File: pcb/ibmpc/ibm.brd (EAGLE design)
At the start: 104 x 74 mm, 43 parts, among them J2 ATX24RH

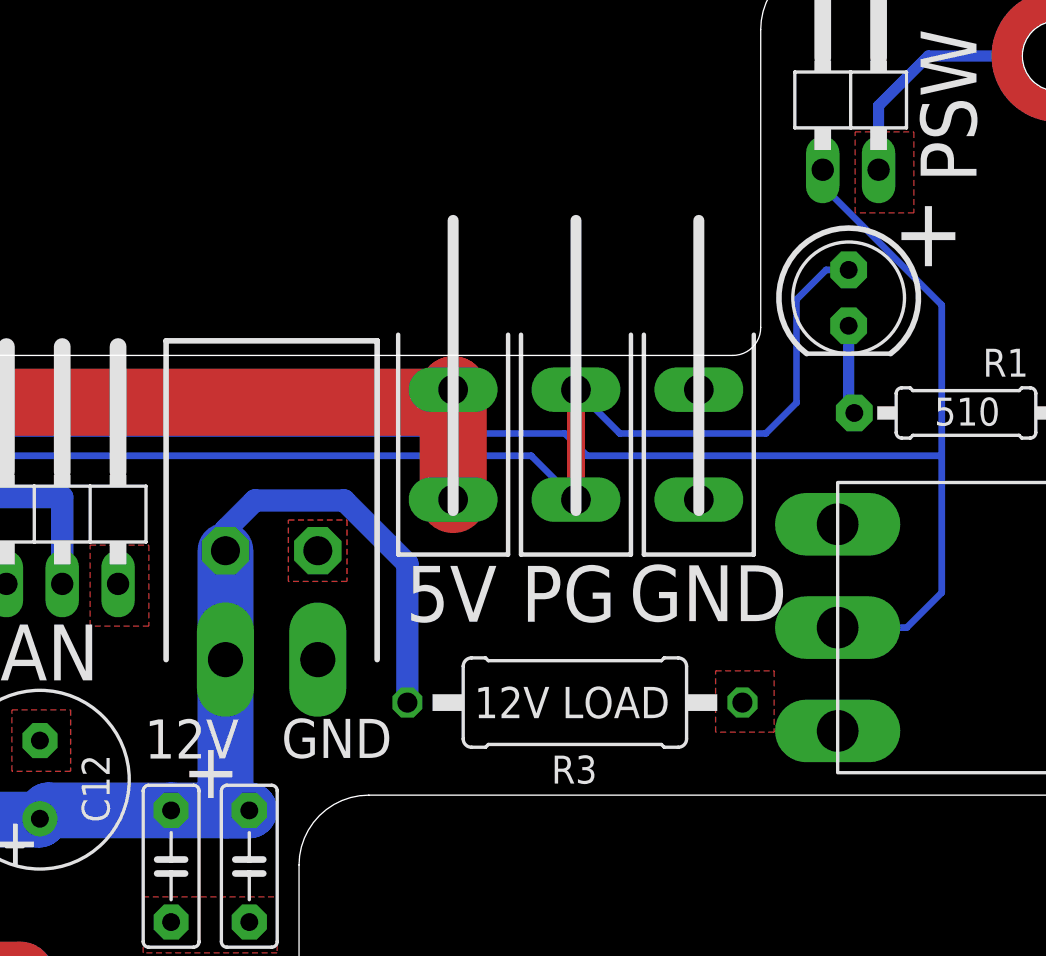
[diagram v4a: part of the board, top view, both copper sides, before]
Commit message: added 12V load resistor and blade
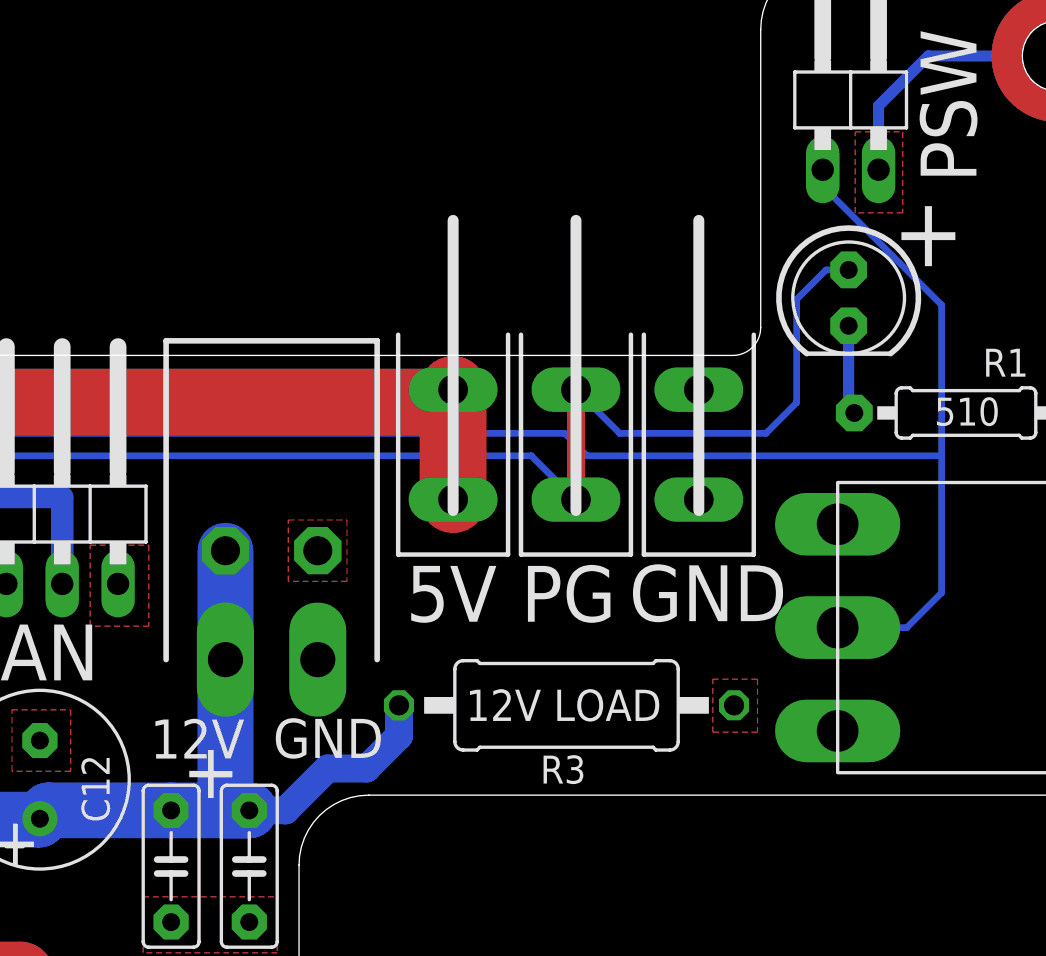
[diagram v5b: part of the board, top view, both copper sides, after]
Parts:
- moved R3 0.40 mm to (77.2, 40.1)
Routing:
- net +12V: track 121.4 -> 113.7 mm
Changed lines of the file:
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@@
 <text x="77.264" y="45.157" size="2.54" layer="25" align="center">PG</text>
 <text x="52.753" y="42.49" size="2.54" layer="25" align="center">FAN</text>
-<text x="60.119" y="38.553" size="1.778" layer="25" align="center">12V</text>
-<text x="66.717" y="38.58" size="1.778" layer="25" rot="R180" align="center">GND</text>
+<text x="60.373" y="38.553" size="1.778" layer="25" align="center">12V</text>
+<text x="66.336" y="38.58" size="1.778" layer="25" rot="R180" align="center">GND</text>
 <rectangle x1="69.469" y1="48.006" x2="74.549" y2="55.753" layer="41"/>
 <rectangle x1="75.184" y1="48.006" x2="80.264" y2="55.753" layer="41"/>
@@
 <text x="47.019" y="40.185" size="2.1844" layer="25" align="center">+</text>
 <text x="38.383" y="43.995" size="2.1844" layer="25" align="center">+</text>
-<text x="77.416" y="40.212" size="1.4224" layer="25" rot="R180" align="center">12V LOAD</text>
+<text x="77.035" y="40.085" size="1.4224" layer="25" rot="R180" align="center">12V LOAD</text>
 </plain>
 <attributes>
@@
 <attribute name="VALUE" x="59.944" y="34.798" size="1.27" layer="27" ratio="10" rot="R270"/>
 </element>
-<element name="R3" library="adafruit_changed" package="0411/15" value="" x="77.548" y="40.21" smashed="yes" rot="R180">
-<attribute name="NAME" x="78.564" y="37.797" size="1.27" layer="25" ratio="10" rot="R180"/>
-<attribute name="VALUE" x="81.1294" y="40.845" size="1.27" layer="27" ratio="10" rot="R180"/>
+<element name="R3" library="adafruit_changed" package="0411/15" value="" x="77.167" y="40.083" smashed="yes" rot="R180">
+<attribute name="NAME" x="78.056" y="37.797" size="1.27" layer="25" ratio="10" rot="R180"/>
+<attribute name="VALUE" x="80.7484" y="40.718" size="1.27" layer="27" ratio="10" rot="R180"/>
 </element>
 <element name="TP2" library="testpad" library_urn="urn:adsk.eagle:library:385" package="P1-13" package3d_urn="urn:adsk.eagle:package:27946/1" value="TPPAD1-13" x="61.654" y="47.117" smashed="yes">
@@
 <polygon width="0.1524" layer="1" thermals="no">
 <vertex x="90.297" y="66.167"/>
-<vertex x="92.964" y="66.167"/>
-<vertex x="92.964" y="62.484"/>
+<vertex x="92.456" y="66.167"/>
+<vertex x="92.456" y="62.484"/>
 <vertex x="90.297" y="62.484"/>
 </polygon>
@@
 </polygon>
 <polygon width="0.1524" layer="1" thermals="no">
-<vertex x="83.947" y="41.656"/>
-<vertex x="86.614" y="41.656"/>
-<vertex x="86.614" y="38.862"/>
-<vertex x="83.947" y="38.862"/>
+<vertex x="83.82" y="41.275"/>
+<vertex x="85.852" y="41.275"/>
+<vertex x="85.852" y="38.862"/>
+<vertex x="83.82" y="38.862"/>
 </polygon>
 </signal>
@@
 <contactref element="TP2" pad="TP"/>
 <wire x1="61.654" y1="42.164" x2="61.654" y2="47.117" width="2.54" layer="16"/>
-<wire x1="61.654" y1="47.117" x2="61.654" y2="48.065" width="1.016" layer="16"/>
-<wire x1="61.654" y1="48.065" x2="62.992" y2="49.403" width="1.016" layer="16"/>
-<wire x1="62.992" y1="49.403" x2="67.056" y2="49.403" width="1.016" layer="16"/>
-<wire x1="67.056" y1="49.403" x2="69.928" y2="46.531" width="1.016" layer="16"/>
-<wire x1="69.928" y1="46.531" x2="69.928" y2="40.21" width="1.016" layer="16"/>
+<wire x1="62.738" y1="35.306" x2="64.389" y2="35.306" width="1.27" layer="16"/>
+<wire x1="64.389" y1="35.306" x2="66.294" y2="37.211" width="1.27" layer="16"/>
+<wire x1="66.294" y1="37.211" x2="68.072" y2="37.211" width="1.27" layer="16"/>
+<wire x1="68.072" y1="37.211" x2="69.547" y2="38.686" width="1.27" layer="16"/>
+<wire x1="69.547" y1="38.686" x2="69.547" y2="40.083" width="1.27" layer="16"/>
 <wire x1="61.654" y1="42.037" x2="61.654" y2="42.164" width="0" layer="19" extent="16-16"/>
 </signal>

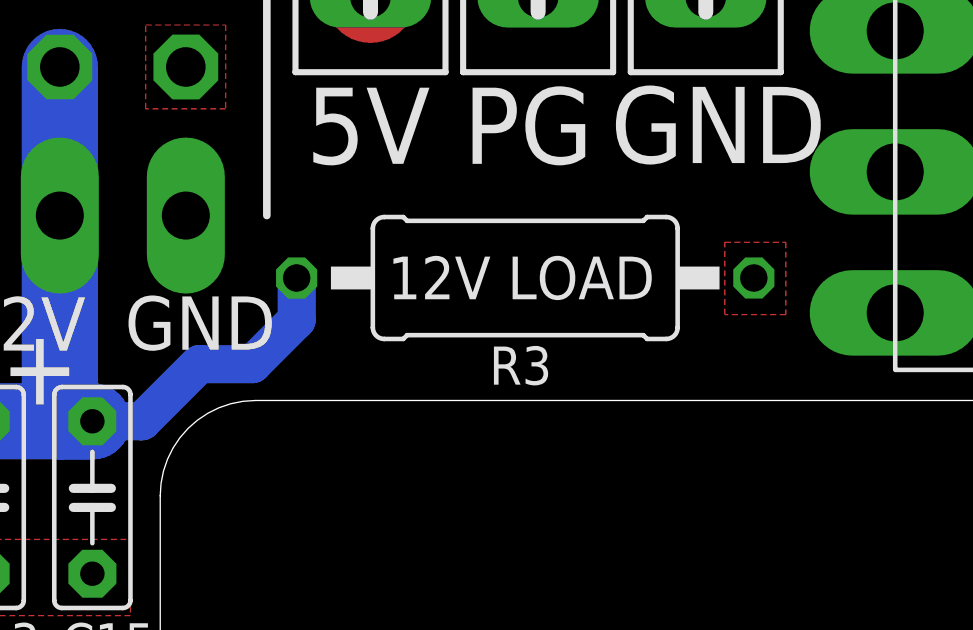
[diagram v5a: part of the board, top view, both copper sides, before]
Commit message: updated with more caps
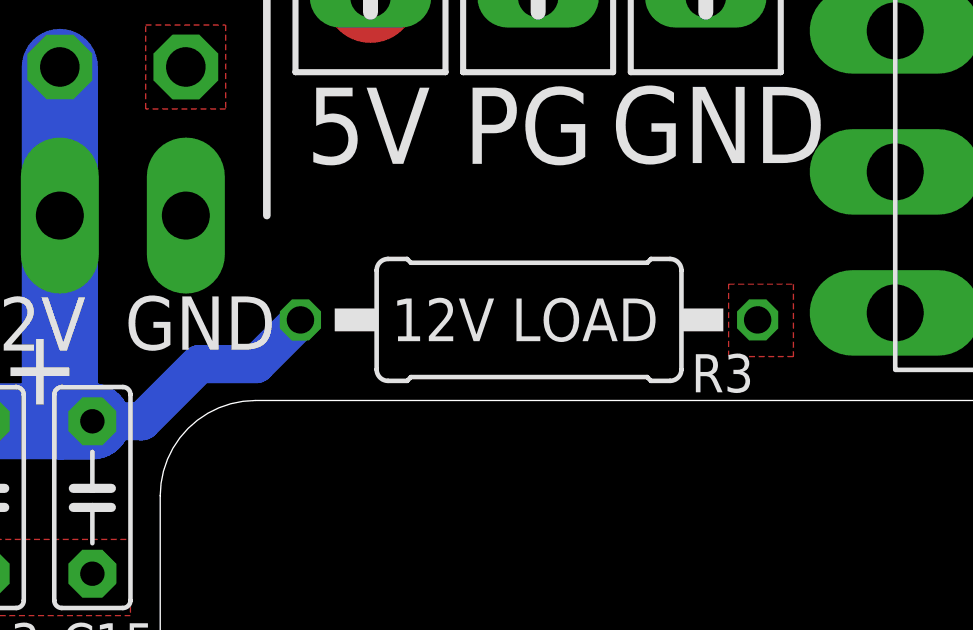
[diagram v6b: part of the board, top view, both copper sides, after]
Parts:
- moved R3 1.40 mm to (77.3, 38.7)
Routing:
- net +12V: track 113.7 -> 112.4 mm
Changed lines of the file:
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@@
 <text x="47.019" y="40.185" size="2.1844" layer="25" align="center">+</text>
 <text x="38.383" y="43.995" size="2.1844" layer="25" align="center">+</text>
-<text x="77.035" y="40.085" size="1.4224" layer="25" rot="R180" align="center">12V LOAD</text>
+<text x="77.162" y="38.688" size="1.4224" layer="25" rot="R180" align="center">12V LOAD</text>
 </plain>
 <attributes>
@@
 <attribute name="VALUE" x="59.944" y="34.798" size="1.27" layer="27" ratio="10" rot="R270"/>
 </element>
-<element name="R3" library="adafruit_changed" package="0411/15" value="" x="77.167" y="40.083" smashed="yes" rot="R180">
-<attribute name="NAME" x="78.056" y="37.797" size="1.27" layer="25" ratio="10" rot="R180"/>
-<attribute name="VALUE" x="80.7484" y="40.718" size="1.27" layer="27" ratio="10" rot="R180"/>
+<element name="R3" library="adafruit_changed" package="0411/15" value="" x="77.294" y="38.686" smashed="yes" rot="R180">
+<attribute name="NAME" x="84.787" y="37.543" size="1.27" layer="25" ratio="10" rot="R180"/>
+<attribute name="VALUE" x="80.8754" y="39.321" size="1.27" layer="27" ratio="10" rot="R180"/>
 </element>
 <element name="TP2" library="testpad" library_urn="urn:adsk.eagle:library:385" package="P1-13" package3d_urn="urn:adsk.eagle:package:27946/1" value="TPPAD1-13" x="61.654" y="47.117" smashed="yes">
@@
 </polygon>
 <polygon width="0.1524" layer="1" thermals="no">
-<vertex x="83.82" y="41.275"/>
-<vertex x="85.852" y="41.275"/>
-<vertex x="85.852" y="38.862"/>
-<vertex x="83.82" y="38.862"/>
+<vertex x="83.947" y="39.878"/>
+<vertex x="86.106" y="39.878"/>
+<vertex x="86.106" y="37.465"/>
+<vertex x="83.947" y="37.465"/>
 </polygon>
 </signal>
@@
 <wire x1="62.738" y1="35.306" x2="64.389" y2="35.306" width="1.27" layer="16"/>
 <wire x1="64.389" y1="35.306" x2="66.294" y2="37.211" width="1.27" layer="16"/>
-<wire x1="66.294" y1="37.211" x2="68.072" y2="37.211" width="1.27" layer="16"/>
-<wire x1="68.072" y1="37.211" x2="69.547" y2="38.686" width="1.27" layer="16"/>
-<wire x1="69.547" y1="38.686" x2="69.547" y2="40.083" width="1.27" layer="16"/>
+<wire x1="66.294" y1="37.211" x2="68.199" y2="37.211" width="1.27" layer="16"/>
+<wire x1="68.199" y1="37.211" x2="69.674" y2="38.686" width="1.27" layer="16"/>
 <wire x1="61.654" y1="42.037" x2="61.654" y2="42.164" width="0" layer="19" extent="16-16"/>
 </signal>
